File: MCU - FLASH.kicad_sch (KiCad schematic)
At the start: 3 parts, among them IC3 MT25QL128ABA1ESE-0SIT

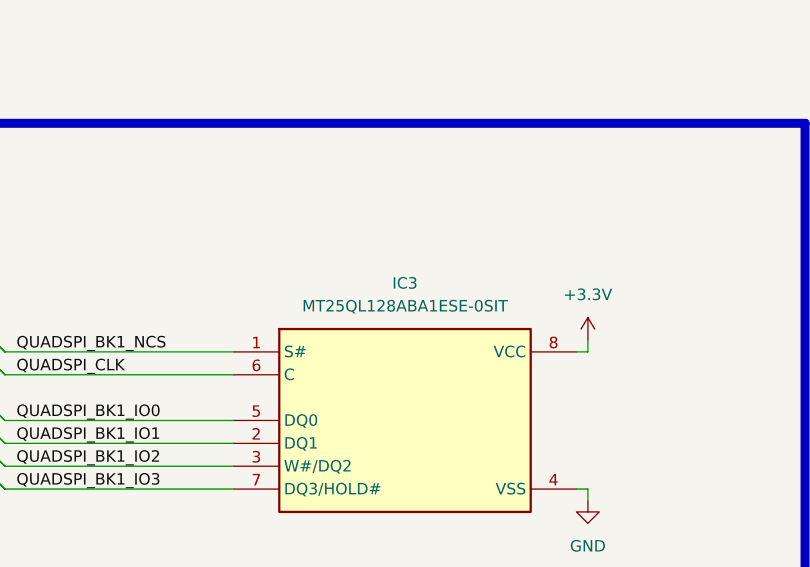
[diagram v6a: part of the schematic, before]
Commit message: designator chagnes and cleanup silkscreen
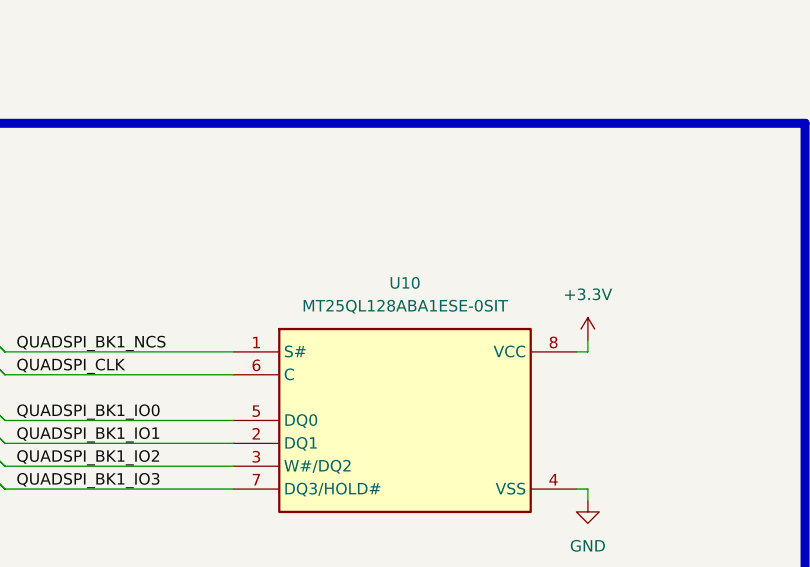
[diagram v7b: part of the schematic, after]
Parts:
- C22: LCSC PN (none) -> C1525
- R15: LCSC PN (none) -> C25744
- U10: renamed from IC3; LCSC PN (none) -> C41359590
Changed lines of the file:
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@@
 		(dnp no)
 		(fields_autoplaced yes)
-		(property "Reference" "IC3"
+		(property "Reference" "U10"
 			(at 262.89 105.41 0)
 			(effects
@@
 		)
 		(property "Supplier Part Number 1" "C41359590"
+			(at 243.84 113.03 0)
+			(effects
+				(font
+					(size 1.27 1.27)
+				)
+				(hide yes)
+			)
+		)
+		(property "LCSC PN" "C41359590"
 			(at 243.84 113.03 0)
 			(effects
@@
 			(project ""
 				(path "/0650c7a8-acba-429c-9f8e-eec0baf0bc1c/fede4c36-00cc-4d3d-b71c-5243ba232202/5d39387f-cfb2-4114-9063-1879c6e2b9e7"
-					(reference "IC3")
+					(reference "U10")
 					(unit 1)
 				)
@@
 			)
 		)
+		(property "LCSC PN" "C1525"
+			(at 153.67 105.41 0)
+			(effects
+				(font
+					(size 1.27 1.27)
+				)
+				(hide yes)
+			)
+		)
 		(pin "1"
 		)
@@
 			(at 153.67 137.16 0)
 			(effects
+				(font
+					(size 1.27 1.27)
+				)
+				(hide yes)
+			)
+		)
+		(property "LCSC PN" "C25744"
+			(at 153.67 137.16 0)
+			(effects
